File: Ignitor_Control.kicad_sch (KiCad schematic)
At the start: 17 parts, among them J14 Ignitor Screw Terminal, K3 G5Q-1, K4 G5Q-1, Q4 BSS138, Q5 BSS138, U12 INA187A1

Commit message: add some comments to clarify ign_resist_read circuitry and implementation
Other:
- note added: "While ign prime switch is on resist read, ign current read will always read 0v"
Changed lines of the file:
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@@
 		(company "Queen's Rocket Engineering Team")
+	)
+	(text "While ign prime switch is on resist read,\nign current read will always read 0v"
+		(exclude_from_sim no)
+		(at 59.182 71.374 0)
+		(effects
+			(font
+				(size 1.27 1.27)
+				(thickness 0.254)
+				(bold yes)
+			)
+			(justify left)
+		)
 	)
 	(text "0A -> 5V\nPick 6A as max current for short detection. Ignitors should pull 3-4A.\nVout_max = REF + 6A * Rsense * Gain\n          = 0 + 6 * 0.025 * 20\n          = 3V\nAt 0A, output should be 0V\n\nI_IGN = V_out / (0.025 * 20)"

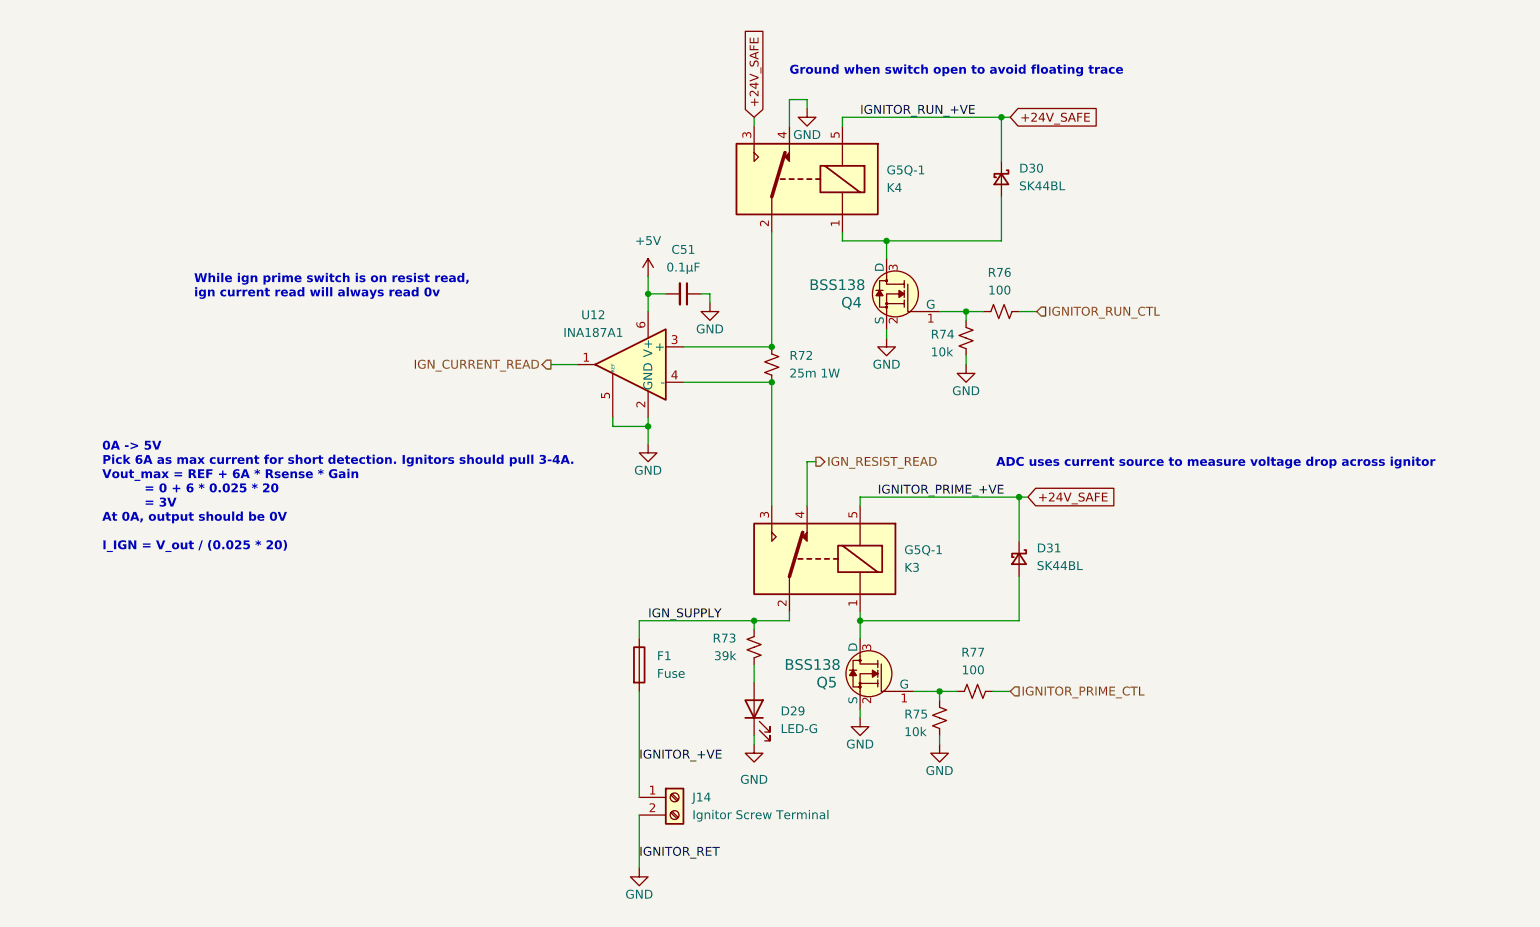
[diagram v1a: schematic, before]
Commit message: add capacitor and resistor footprints
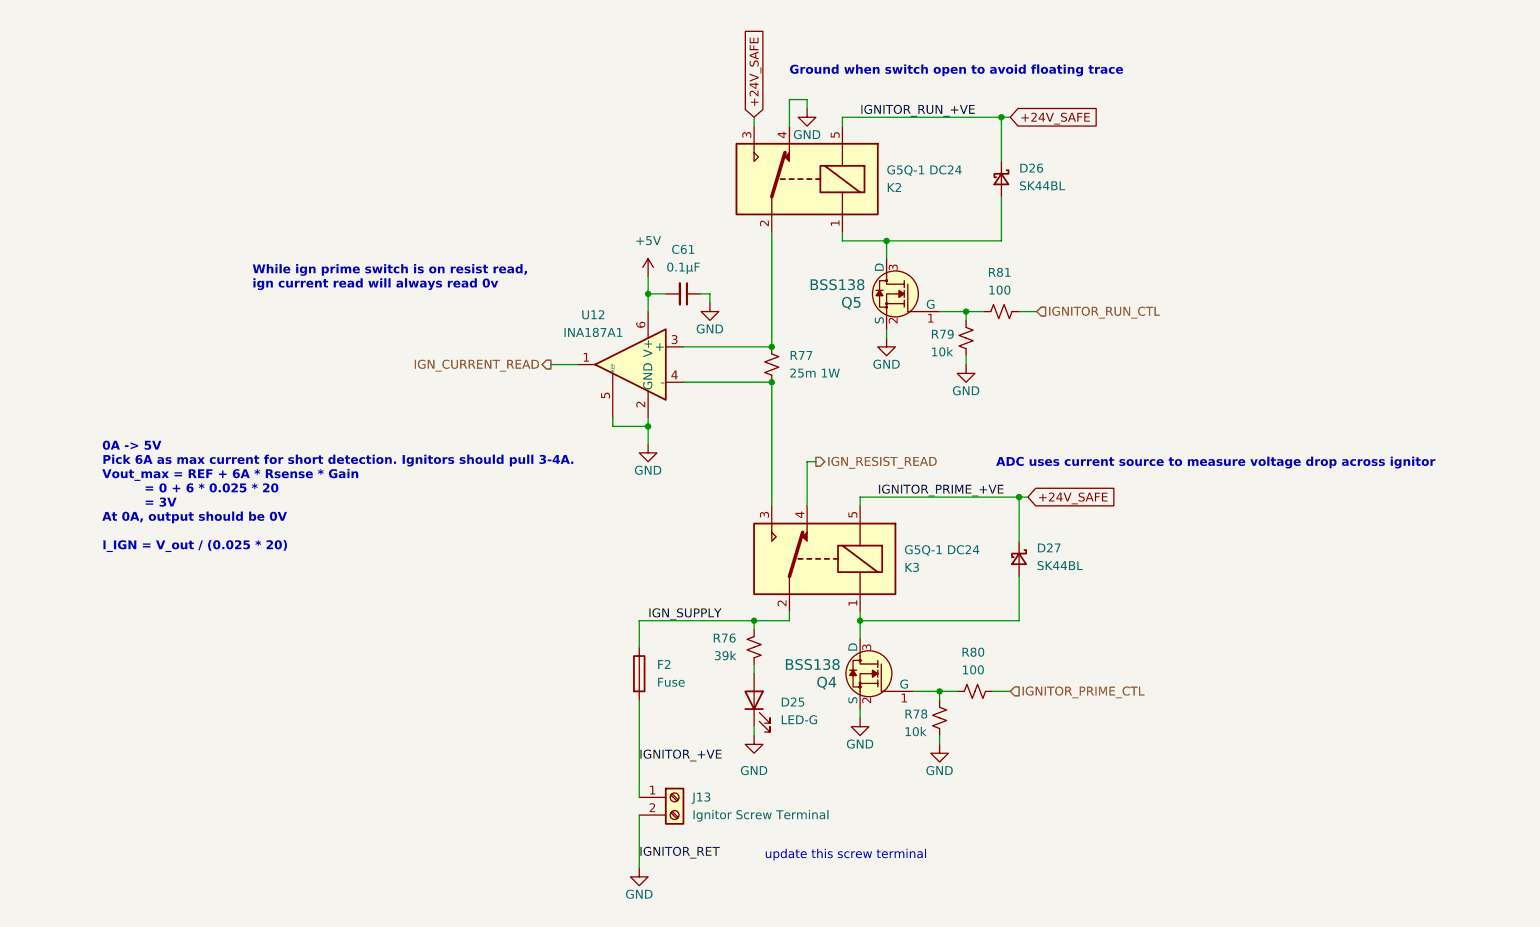
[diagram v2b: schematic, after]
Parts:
- C61: renamed from C51; LCSC C1525 -> C307331
- K2: renamed from K4; value G5Q-1 -> G5Q-1 DC24
- K3: value G5Q-1 -> G5Q-1 DC24
- renumbered D29 to D25, D30 to D26, D31 to D27, F1 to F2, J14 to J13, Q5 to Q4, Q4 to Q5, R73 to R76, R72 to R77, R75 to R78, R74 to R79, R77 to R80, R76 to R81
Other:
- note added: "update this screw terminal"
- moved on the sheet: D25, F2

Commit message: change connectors and more progress on pcb
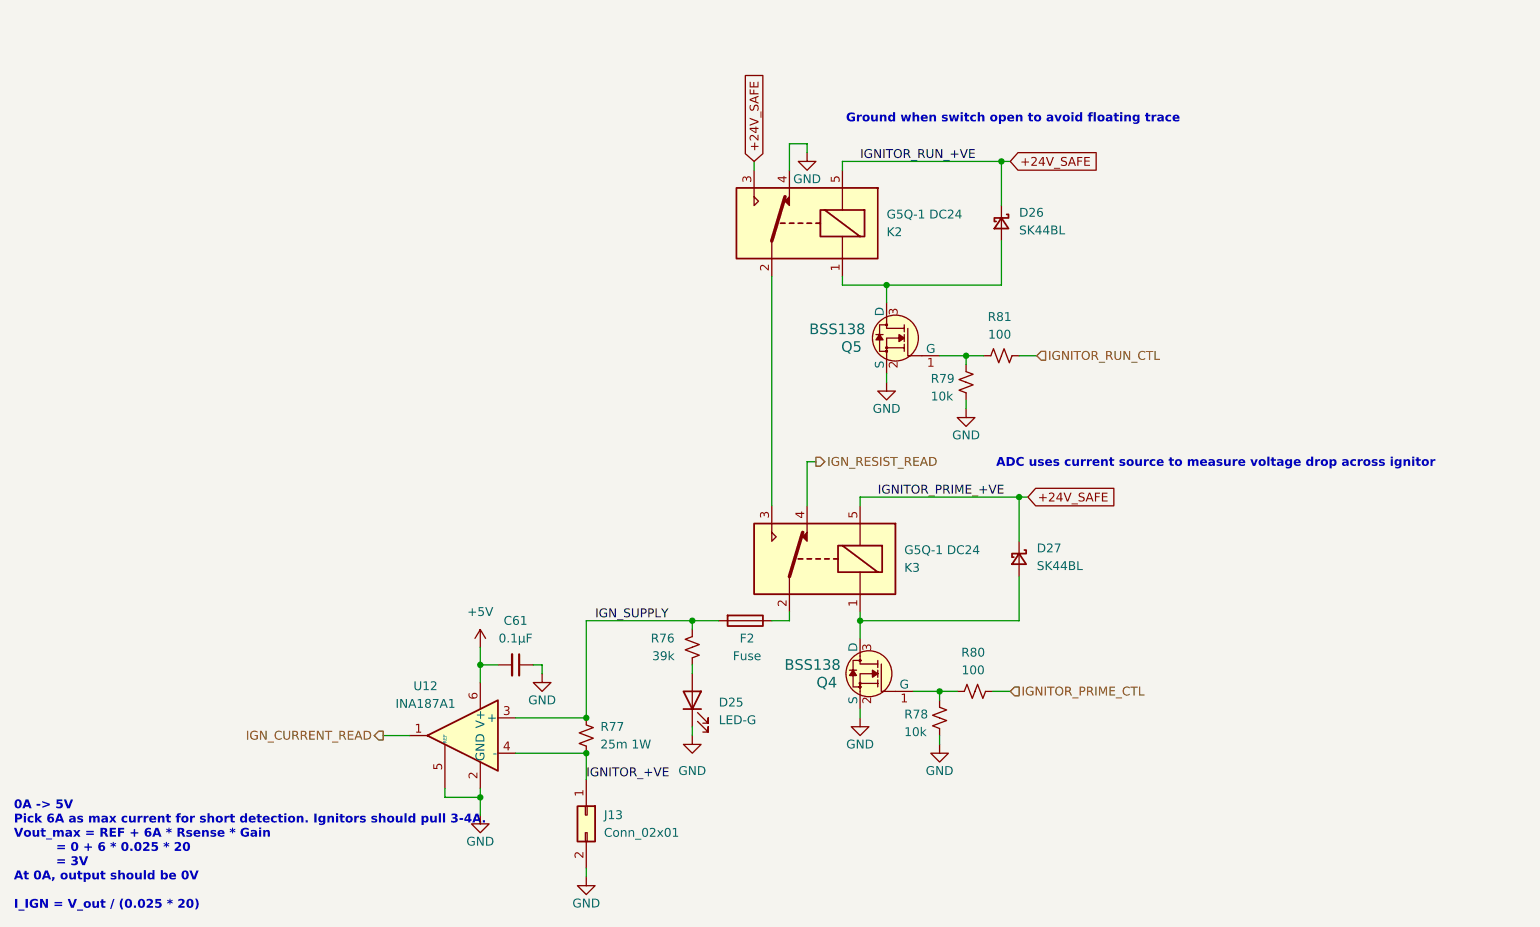
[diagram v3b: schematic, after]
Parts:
- removed J13: Ignitor Screw Terminal, TerminalBlock_4Ucon:TerminalBlock_4Ucon_1x02_P3.50mm_Vertical, symbol Connector:Screw_Terminal_01x02
- added J13: Conn_02x01, Connector_Molex:Molex_Mini-Fit_Jr_5566-02A_2x01_P4.20mm_Vertical, symbol Connector_Generic:Conn_02x01
- R77: LCSC C723507 -> (none)
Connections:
- net GND: now also J13.2 (Pin_2)
- net IGNITOR_+VE: now also R77.2, U12.4 (-), J13.1 (Pin_1); no longer F2.2
- net IGN_SUPPLY: now also F2.2, R77.1, U12.3 (+); no longer F2.1, K3.2
- new net: K2.2, K3.3
- new net: F2.1, K3.2
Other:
- note removed: "While ign prime switch is on resist read, ign current read will always read 0v"
- note removed: "update this screw terminal"
- moved on the sheet: C61, D25, D26, F2, K2, Q5, R76, R77, R79, R81, U12

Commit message: change clamping resistors on tc adcs for lower leakage current
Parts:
- renumbered R77 to R75, R78 to R77, R79 to R78, R80 to R79, R81 to R80
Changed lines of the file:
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@@
 		(on_board yes)
 		(dnp no)
-		(property "Reference" "R77"
+		(property "Reference" "R75"
 			(at 117.602 134.62 0)
 			(effects
@@
 			(project ""
 				(path "/226c5870-4123-4efa-a2b3-b42d02f59bb7/4e09186f-4067-4c22-bbd5-0048a728fd95"
-					(reference "R77")
+					(reference "R75")
 					(unit 1)
 				)
@@
 		(on_board yes)
 		(dnp no)
-		(property "Reference" "R81"
+		(property "Reference" "R80"
 			(at 175.006 75.692 90)
 			(effects
@@
 			(project "panda"
 				(path "/226c5870-4123-4efa-a2b3-b42d02f59bb7/4e09186f-4067-4c22-bbd5-0048a728fd95"
-					(reference "R81")
+					(reference "R80")
 					(unit 1)
 				)
@@
 		(on_board yes)
 		(dnp no)
-		(property "Reference" "#PWR0168"
+		(property "Reference" "#PWR0169"
 			(at 170.18 95.25 0)
 			(effects
@@
 			(project "panda"
 				(path "/226c5870-4123-4efa-a2b3-b42d02f59bb7/4e09186f-4067-4c22-bbd5-0048a728fd95"
-					(reference "#PWR0168")
+					(reference "#PWR0169")
 					(unit 1)
 				)
@@
 		(dnp no)
 		(fields_autoplaced yes)
-		(property "Reference" "#PWR0163"
+		(property "Reference" "#PWR0164"
 			(at 130.81 142.24 0)
 			(effects
@@
 			(project "panda"
 				(path "/226c5870-4123-4efa-a2b3-b42d02f59bb7/4e09186f-4067-4c22-bbd5-0048a728fd95"
-					(reference "#PWR0163")
+					(reference "#PWR0164")
 					(unit 1)
 				)
@@
 		(on_board yes)
 		(dnp no)
-		(property "Reference" "#PWR0166"
+		(property "Reference" "#PWR0167"
 			(at 158.75 91.44 0)
 			(effects
@@
 			(project "panda"
 				(path "/226c5870-4123-4efa-a2b3-b42d02f59bb7/4e09186f-4067-4c22-bbd5-0048a728fd95"
-					(reference "#PWR0166")
+					(reference "#PWR0167")
 					(unit 1)
 				)
@@
 		(on_board yes)
 		(dnp no)
-		(property "Reference" "#PWR0159"
+		(property "Reference" "#PWR0163"
 			(at 115.57 162.56 0)
 			(effects
@@
 			(project "nexus"
 				(path "/226c5870-4123-4efa-a2b3-b42d02f59bb7/4e09186f-4067-4c22-bbd5-0048a728fd95"
-					(reference "#PWR0159")
+					(reference "#PWR0163")
 					(unit 1)
 				)
@@
 		(on_board yes)
 		(dnp no)
-		(property "Reference" "R79"
+		(property "Reference" "R78"
 			(at 165.1 84.582 0)
 			(effects
@@
 			(project "panda"
 				(path "/226c5870-4123-4efa-a2b3-b42d02f59bb7/4e09186f-4067-4c22-bbd5-0048a728fd95"
-					(reference "R79")
+					(reference "R78")
 					(unit 1)
 				)
@@
 		(on_board yes)
 		(dnp no)
-		(property "Reference" "#PWR0165"
+		(property "Reference" "#PWR0166"
 			(at 154.94 139.7 0)
 			(effects
@@
 			(project "nexus"
 				(path "/226c5870-4123-4efa-a2b3-b42d02f59bb7/4e09186f-4067-4c22-bbd5-0048a728fd95"
-					(reference "#PWR0165")
+					(reference "#PWR0166")
 					(unit 1)
 				)
@@
 		(on_board yes)
 		(dnp no)
-		(property "Reference" "#PWR0164"
+		(property "Reference" "#PWR0165"
 			(at 147.32 58.42 0)
 			(effects
@@
 			(project "panda"
 				(path "/226c5870-4123-4efa-a2b3-b42d02f59bb7/4e09186f-4067-4c22-bbd5-0048a728fd95"
-					(reference "#PWR0164")
+					(reference "#PWR0165")
 					(unit 1)
 				)
@@
 		(on_board yes)
 		(dnp no)
-		(property "Reference" "R78"
+		(property "Reference" "R77"
 			(at 161.29 132.842 0)
 			(effects
@@
 			(project "panda"
 				(path "/226c5870-4123-4efa-a2b3-b42d02f59bb7/4e09186f-4067-4c22-bbd5-0048a728fd95"
-					(reference "R78")
+					(reference "R77")
 					(unit 1)
 				)
@@
 		(on_board yes)
 		(dnp no)
-		(property "Reference" "#PWR0167"
+		(property "Reference" "#PWR0168"
 			(at 166.37 143.51 0)
 			(effects
@@
 			(project "panda"
 				(path "/226c5870-4123-4efa-a2b3-b42d02f59bb7/4e09186f-4067-4c22-bbd5-0048a728fd95"
-					(reference "#PWR0167")
+					(reference "#PWR0168")
 					(unit 1)
 				)
@@
 		(on_board yes)
 		(dnp no)
-		(property "Reference" "R80"
+		(property "Reference" "R79"
 			(at 171.196 123.952 90)
 			(effects
@@
 			(project "panda"
 				(path "/226c5870-4123-4efa-a2b3-b42d02f59bb7/4e09186f-4067-4c22-bbd5-0048a728fd95"
-					(reference "R80")
+					(reference "R79")
 					(unit 1)
 				)

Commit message: Update version number in KiCad files
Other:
- title: Ignitor Control -> PANDA
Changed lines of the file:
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@@
 	(paper "A4")
 	(title_block
-		(title "Ignitor Control")
-		(rev "1.0.0")
+		(title "PANDA")
+		(date "2025-12-21")
+		(rev "3.0.0")
 		(company "Queen's Rocket Engineering Team")
 	)

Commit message: Update with new production files. Change CSA to INA187A2 (from A1 skew) for LCSC availability reasons.
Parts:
- R75: value 25m 1W -> 10m 1W
- U12: value INA187A1 -> INA187A2; LCSC C49262296 -> C49262295
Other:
- note added: "0A -> 5V Pick 6A as max current for short detection. Ignitors should pull 3-4A. Vout_max = REF + 6A * Rsense * Gain = 0 + 6 * 0.01 * 50 = 3V At 0A, output should be 0V I_IGN = V_out / (0.01 * 50)"
- note removed: "0A -> 5V Pick 6A as max current for short detection. Ignitors should pull 3-4A. Vout_max = REF + 6A * Rsense * Gain = 0 + 6 * 0.025 * 20 = 3V At 0A, output should be 0V I_IGN = V_out / (0.025 * 20)"
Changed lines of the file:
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@@
 		(company "Queen's Rocket Engineering Team")
 	)
-	(text "0A -> 5V\nPick 6A as max current for short detection. Ignitors should pull 3-4A.\nVout_max = REF + 6A * Rsense * Gain\n          = 0 + 6 * 0.025 * 20\n          = 3V\nAt 0A, output should be 0V\n\nI_IGN = V_out / (0.025 * 20)"
+	(text "0A -> 5V\nPick 6A as max current for short detection. Ignitors should pull 3-4A.\nVout_max = REF + 6A * Rsense * Gain\n          = 0 + 6 * 0.01 * 50\n          = 3V\nAt 0A, output should be 0V\n\nI_IGN = V_out / (0.01 * 50)"
 		(exclude_from_sim no)
 		(at 33.274 153.162 0)
@@
 			)
 		)
-		(property "Value" "25m 1W"
+		(property "Value" "10m 1W"
 			(at 117.602 137.16 0)
 			(effects
@@
 			)
 		)
-		(property "Value" "INA187A1"
+		(property "Value" "INA187A2"
 			(at 92.456 131.318 0)
 			(effects
@@
 			)
 		)
-		(property "LCSC" "C49262296"
+		(property "LCSC" "C49262295"
 			(at 97.79 135.89 0)
 			(effects
